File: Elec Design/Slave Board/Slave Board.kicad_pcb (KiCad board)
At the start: 2 copper layers, 81.3 x 358.6 mm, 93 parts, among them J3 OSTTC030162, J5 OSTTC030162, J6 0022232041, J7 Conn_ARM_JTAG_SWD_10, J8 OSTTC020162, J9 OSTTC020162, M1 Val**, M2 Val**, M3 Val**, M4 Val**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

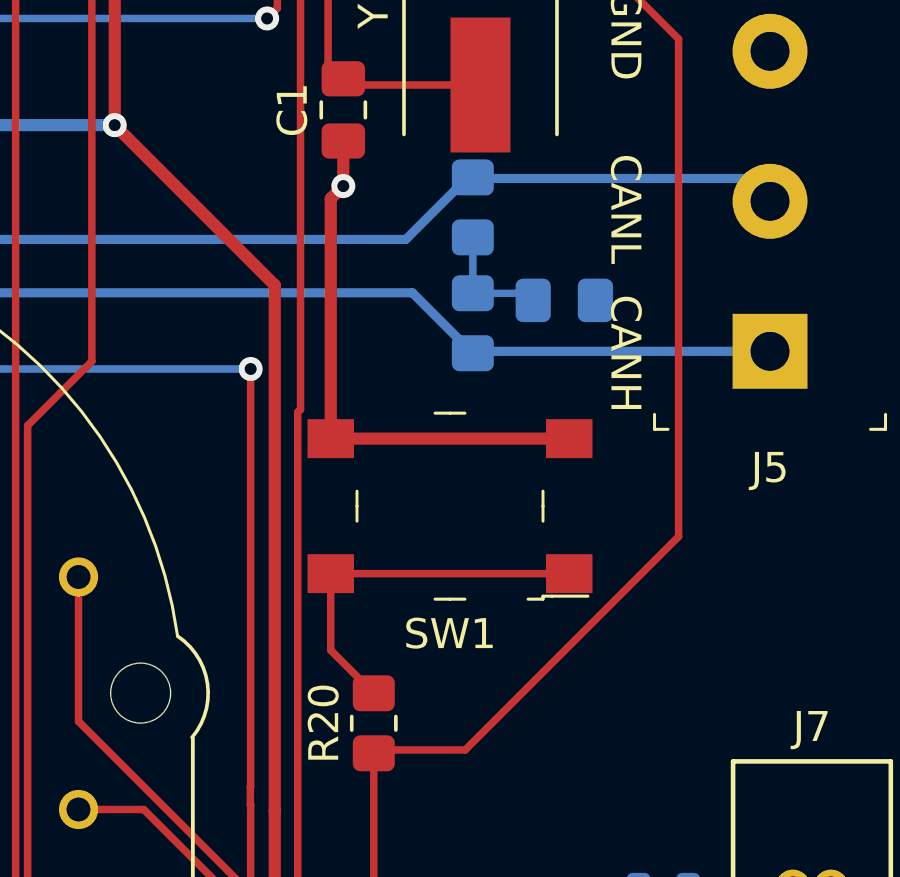
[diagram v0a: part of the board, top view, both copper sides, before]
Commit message: lining up with JLC parts
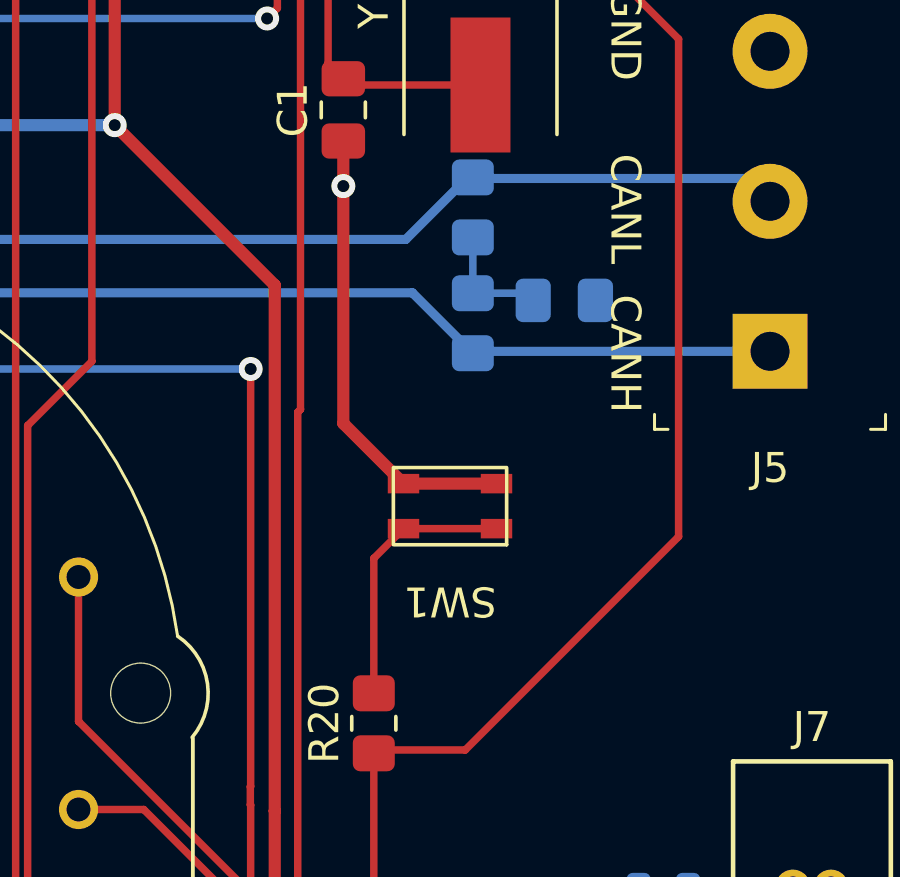
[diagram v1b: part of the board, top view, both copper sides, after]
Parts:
- SW1: footprint digikey-footprints:Switch_Tactile_SMD_6x6mm_PTS645 -> Switches:SW_SPST_ SKRPASE010
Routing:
- net Net-(R20-Pad2): track 12.5 -> 9.00 mm
- net GND: track 104.4 -> 101.7 mm

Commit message: further JLC alignment
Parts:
- J3, J5: value OSTTC030162 -> ~
- M1, M2, M3, M4: value Val** -> VID28-05
- U1: value LPC11C22_24-LQFP48 -> LPC11C24-LQFP48

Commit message: further bom alignment
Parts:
- C1, C10, C11, C12, C13, C16, C18, C19, C2, C21, C22, C23, C24, C3, C4, C5, C6, C7, C8, C9: footprint Capacitor_SMD:C_0805_2012Metric_Pad1.18x1.45mm_HandSolder -> Capacitor_SMD:C_0603_1608Metric
- C27, C28: value 0.1uF -> 100nF
- J3, J5: footprint digikey-footprints:Term_Block_1x3_P5mm -> TerminalBlock_Phoenix:TerminalBlock_Phoenix_PT-1,5-3-5.0-H_1x03_P5.00mm_Horizontal
- J6: value 0022232041 -> ~; footprint digikey-footprints:PinHeader_1x4_P2.54mm_Drill1.02mm -> Connector_PinHeader_2.54mm:PinHeader_1x04_P2.54mm_Vertical
- J7: footprint 10 pin jtag:CONN_3220-10-0100-00_CNC -> digikey-footprints:PinHeader_2x5_P1.27mm_Drill.7mm
- J8, J9: value OSTTC020162 -> ~; footprint digikey-footprints:Term_Block_1x2_P5mm -> TerminalBlock_Phoenix:TerminalBlock_Phoenix_PT-1,5-2-5.0-H_1x02_P5.00mm_Horizontal
- L1: footprint NR6028T4R7M:IND_NR6028T4R7M -> Inductors:IND_NR6028T4R7M
- R10, R11, R12, R13, R17, R18, R20, R29, R30, R5, R6, R7, R8, R9: footprint Resistor_SMD:R_0805_2012Metric_Pad1.20x1.40mm_HandSolder -> Resistor_SMD:R_0603_1608Metric
- R22: footprint Resistor_SMD:R_1206_3216Metric_Pad1.30x1.75mm_HandSolder -> Resistor_SMD:R_0603_1608Metric
- SW1: footprint Switches:SW_SPST_ SKRPASE010 -> Button_Switch_SMD:SW_SPST_PTS810
- U14: footprint BD9E302EFJ-E2:HTSOP-J8_ROM -> Buck Converter:HTSOP-J8_ROM
- moved Y1 9.86 mm to (261.6, 213.4)
- moved C1 8.87 mm to (256.5, 210.8)
- moved R20 3.56 mm to (269.7, 233.3)
- moved C2 2.29 mm to (259.3, 203.5)
- moved C3 2.29 mm to (261.6, 203.5)
- moved SW1 1.48 mm to (270.2, 226.0)
- moved J3 0.78 mm to (208.8, 211.4)
- moved C33 0.76 mm to (211.8, 171.2)
- moved D5 0.76 mm to (208.8, 192.3)
- moved J5 0.72 mm to (278.9, 221.4)
- moved J8 0.51 mm to (208.8, 199.9)
- moved J9 0.50 mm to (278.9, 204.9)
- turned J6 to 0 degrees
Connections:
- R20 pad 2: Net-(R20-Pad2) -> Net-(SW1-A)
- SW1 pad 1: Net-(R20-Pad2) -> Net-(SW1-A)
- SW1 pad 2: Net-(R20-Pad2) -> GND
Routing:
- net /RESET: track 76.5 -> 61.9 mm
- net +3.3V: track 813.5 -> 825.1 mm
- net Net-(SW1-A): track 0.00 -> 10.3 mm
- net Net-(R20-Pad2): track 9.00 -> 0.00 mm
- net GND: track 101.7 -> 94.6 mm, vias 24 -> 25
- net Net-(U1-XTALOUT): track 24.2 -> 17.8 mm, vias 3 -> 0
- net Net-(U1-XTALIN): track 26.1 -> 21.1 mm, vias 2 -> 0
- net VBUS: track 110.1 -> 107.9 mm
- net /HAll B Hour - 2: track 184.9 -> 182.7 mm
- net /CW/~{CCWC} - 2: track 127.8 -> 126.3 mm
- net /Driver Reset: track 243.9 -> 245.2 mm
- net /CANL: track 114.0 -> 112.9 mm
- net /HAll B Hour - 1: track 81.7 -> 82.7 mm
- net Net-(D5-A): track 19.1 -> 18.1 mm
- net Net-(U1-PIO3_0/~{DTR}): track 2.68 -> 3.31 mm
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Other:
- board text added: "Slave Board V1.1"

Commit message: minor bom changes
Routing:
- net +3.3V: track 825.1 -> 827.1 mm
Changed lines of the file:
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@@
 			)
 		)
+		(property "JLC PN" "C3819953"
+			(at 0 0 -90)
+			(unlocked yes)
+			(layer "F.Fab")
+			(hide yes)
+			(effects
+				(font
+					(size 1 1)
+					(thickness 0.15)
+				)
+			)
+		)
 		(sheetname "Root")
 		(sheetfile "Slave Board.kicad_sch")
@@
 			)
 		)
-		(property "MPN" "LPC11C24FBD48"
+		(property "MPN" "C1020252"
 			(at 0 0 180)
 			(unlocked yes)
@@
 			)
 		)
+		(property "JLC PN" "C2992620"
+			(at 0 0 -90)
+			(unlocked yes)
+			(layer "F.Fab")
+			(hide yes)
+			(effects
+				(font
+					(size 1 1)
+					(thickness 0.15)
+				)
+			)
+		)
 		(property ki_fp_filters "C_*")
 		(sheetname "Root")
@@
 			)
 		)
+		(property "JLC PN" "C3819953"
+			(at 0 0 90)
+			(unlocked yes)
+			(layer "F.Fab")
+			(hide yes)
+			(effects
+				(font
+					(size 1 1)
+					(thickness 0.15)
+				)
+			)
+		)
 		(sheetname "Root")
 		(sheetfile "Slave Board.kicad_sch")
@@
 			)
 		)
-		(property "Datasheet" "https://www.diodes.com/assets/Datasheets/B320AE/B340AE.pdf"
+		(property "Datasheet" "https://www.lcsc.com/datasheet/lcsc_datasheet_2307101649_MDD-Microdiode-Electronics-B340A_C64982.pdf"
 			(at 0 0 90)
 			(unlocked yes)
@@
 			)
 		)
-		(property "MPN" "B340AE"
+		(property "MPN" "C64982"
 			(at 0 0 0)
 			(layer "F.Fab")
@@
 			)
 		)
+		(property "JLC PN" "C2992620"
+			(at 0 0 0)
+			(unlocked yes)
+			(layer "F.Fab")
+			(hide yes)
+			(effects
+				(font
+					(size 1 1)
+					(thickness 0.15)
+				)
+			)
+		)
 		(property ki_fp_filters "C_*")
 		(sheetname "Root")
@@
 			)
 		)
+		(property "MPN" "C2891841"
+			(at 0 0 90)
+			(unlocked yes)
+			(layer "F.Fab")
+			(hide yes)
+			(effects
+				(font
+					(size 1 1)
+					(thickness 0.15)
+				)
+			)
+		)
 		(property ki_fp_filters "SOT?23*")
 		(sheetname "Root")
@@
 		(tags "resistor")
 		(property "Reference" "R30"
-			(at 0 -1.43 0)
+			(at 0.127 1.651 0)
 			(layer "F.SilkS")
 			(effects
@@
 		(tags "capacitor")
 		(property "Reference" "C24"
-			(at 0 -1.43 90)
+			(at 0.127 1.651 90)
 			(layer "F.SilkS")
 			(effects
@@
 		(tags "capacitor")
 		(property "Reference" "C16"
-			(at 0 -1.43 0)
+			(at 0 1.524 0)
 			(layer "F.SilkS")
 			(effects
@@
 		(tags "capacitor")
 		(property "Reference" "C18"
-			(at 0 -1.43 180)
+			(at 0 1.524 180)
 			(layer "F.SilkS")
 			(effects
@@
 		(tags "capacitor")
 		(property "Reference" "C21"
-			(at 0 -1.43 90)
+			(at 0.127 1.524 90)
 			(layer "F.SilkS")
 			(effects
@@
 			)
 		)
+		(property "MPN" "C919448"
+			(at 0 0 90)
+			(unlocked yes)
+			(layer "F.Fab")
+			(hide yes)
+			(effects
+				(font
+					(size 1 1)
+					(thickness 0.15)
+				)
+			)
+		)
+		(property "JLC PN" "C919448"
+			(at 0 0 90)
+			(unlocked yes)
+			(layer "F.Fab")
+			(hide yes)
+			(effects
+				(font
+					(size 1 1)
+					(thickness 0.15)
+				)
+			)
+		)
 		(property ki_fp_filters "HTSOP-J8_ROM HTSOP-J8_ROM-M HTSOP-J8_ROM-L")
 		(sheetname "Root")
@@
 		(tags "capacitor")
 		(property "Reference" "C5"
-			(at 0 -1.43 180)
+			(at 0.127 1.397 180)
 			(layer "F.SilkS")
 			(effects
@@
 			)
 		)
+		(property "JLC PN" "C77758"
+			(at 0 0 180)
+			(unlocked yes)
+			(layer "F.Fab")
+			(hide yes)
+			(effects
+				(font
+					(size 1 1)
+					(thickness 0.15)
+				)
+			)
+		)
 		(property ki_fp_filters "Choke_* *Coil* Inductor_* L_*")
 		(sheetname "Root")
@@
 			)
 		)
-		(property "MPN" "PTS810SJS250SMTRLFS"
+		(property "MPN" "C221897"
 			(at 0 0 180)
 			(unlocked yes)
@@
 			)
 		)
-		(property "Datasheet" "https://connect.kemet.com:7667/gateway/IntelliData-ComponentDocumentation/1.0/download/datasheet/C0603C104K5RECAUTO"
+		(property "Datasheet" ""
 			(at 0 0 0)
 			(unlocked yes)
@@
 			)
 		)
-		(property "JLC?" "N"
+		(property "MPN" "GRM188R6YA106MA73J"
 			(at 0 0 0)
 			(layer "F.Fab")
@@
 			)
 		)
-		(property "MPN" "C0603C104K5RECAUTO"
+		(property "Rated V" "35V"
 			(at 0 0 0)
 			(layer "F.Fab")
@@
 			)
 		)
-		(property "Rated V" "50V"
+		(property "JLC PN" "C2244191"
 			(at 0 0 0)
+			(unlocked yes)
 			(layer "F.Fab")
 			(hide yes)
@@
 			)
 		)
+		(property "JLC PN" "C3816891"
+			(at 0 0 90)
+			(unlocked yes)
+			(layer "F.Fab")
+			(hide yes)
+			(effects
+				(font
+					(size 1 1)
+					(thickness 0.15)
+				)
+			)
+		)
 		(sheetname "Root")
 		(sheetfile "Slave Board.kicad_sch")
@@
 			)
 		)
+		(property "JLC PN" "C2975357"
+			(at 0 0 -90)
+			(unlocked yes)
+			(layer "F.Fab")
+			(hide yes)
+			(effects
+				(font
+					(size 1 1)
+					(thickness 0.15)
+				)
+			)
+		)
+		(property "MPN" "C2975357"
+			(at 0 0 -90)
+			(unlocked yes)
+			(layer "F.Fab")
+			(hide yes)
+			(effects
+				(font
+					(size 1 1)
+					(thickness 0.15)
+				)
+			)
+		)
 		(property ki_fp_filters "Crystal*")
 		(sheetname "Root")
@@
 		(tags "capacitor")
 		(property "Reference" "C3"
-			(at 0 -1.43 90)
+			(at 0.173 1.651 90)
 			(layer "F.SilkS")
 			(effects
@@
 			)
 		)
+		(property "JLC PN" "C3816891"
+			(at 0 0 -90)
+			(unlocked yes)
+			(layer "F.Fab")
+			(hide yes)
+			(effects
+				(font
+					(size 1 1)
+					(thickness 0.15)
+				)
+			)
+		)
 		(sheetname "Root")
 		(sheetfile "Slave Board.kicad_sch")
@@
 		(tags "resistor")
 		(property "Reference" "R13"
-			(at 0 1.43 0)
+			(at 0 -1.524 0)
 			(layer "B.SilkS")
 			(effects
@@
 		(tags "resistor")
 		(property "Reference" "R5"
-			(at 0 1.43 90)
+			(at 0.127 -1.524 90)
 			(layer "B.SilkS")
 			(effects
@@
 		(tags "resistor")
 		(property "Reference" "R12"
-			(at 0 1.43 0)
+			(at 0 -1.651 0)
 			(layer "B.SilkS")
 			(effects
@@
 		(tags "resistor")
 		(property "Reference" "R8"
-			(at 0 1.43 0)
+			(at 0 -1.397 0)
 			(layer "B.SilkS")
 			(effects
@@
 	)
 	(segment
+		(start 206.8575 151.342)
+		(end 206.8575 149.4405)
+		(width 0.4064)
+		(layer "B.Cu")
+		(net 4)
+	)
+	(segment
 		(start 263.398 149.352)
 		(end 264.938 149.352)
@@
 	)
 	(segment
+		(start 206.8575 149.4405)
+		(end 206.769 149.352)
+		(width 0.4064)
+		(layer "B.Cu")
+		(net 4)
+	)
+	(segment
 		(start 263.398 154.686)
 		(end 263.906 155.194)
@@
 	)
 	(segment
-		(start 243.4805 194.14)
-		(end 243.459 194.1615)
-		(width 0.2)
-		(layer "F.Cu")
-		(net 5)
-	)
-	(segment
-		(start 242.593 194.9435)
-		(end 242.593 198.778)
+		(start 243.4805 194.056)
+		(end 242.443 195.0935)
 		(width 0.2)
 		(layer "F.Cu")
@@
 	)
 	(segment
-		(start 243.459 199.644)
-		(end 244.106 200.291)
+		(start 244.106 200.291)
+		(end 244.106 200.30167)
 		(width 0.2)
 		(layer "F.Cu")
@@
 	)
 	(segment
-		(start 243.4805 194.056)
-		(end 243.4805 194.14)
+		(start 243.4805 194.14)
+		(end 243.459 194.1615)
 		(width 0.2)
 		(layer "F.Cu")
@@
 	)
 	(segment
-		(start 242.593 198.778)
-		(end 243.459 199.644)
+		(start 242.443 195.0935)
+		(end 242.443 198.628)
 		(width 0.2)
 		(layer "F.Cu")
@@
 	)
 	(segment
-		(start 244.106 200.291)
-		(end 244.106 200.30167)
+		(start 242.443 198.628)
+		(end 244.106 200.291)
 		(width 0.2)
 		(layer "F.Cu")
@@
 	(segment
 		(start 243.4805 194.056)
-		(end 242.593 194.9435)
+		(end 243.4805 194.14)
 		(width 0.2)
 		(layer "F.Cu")

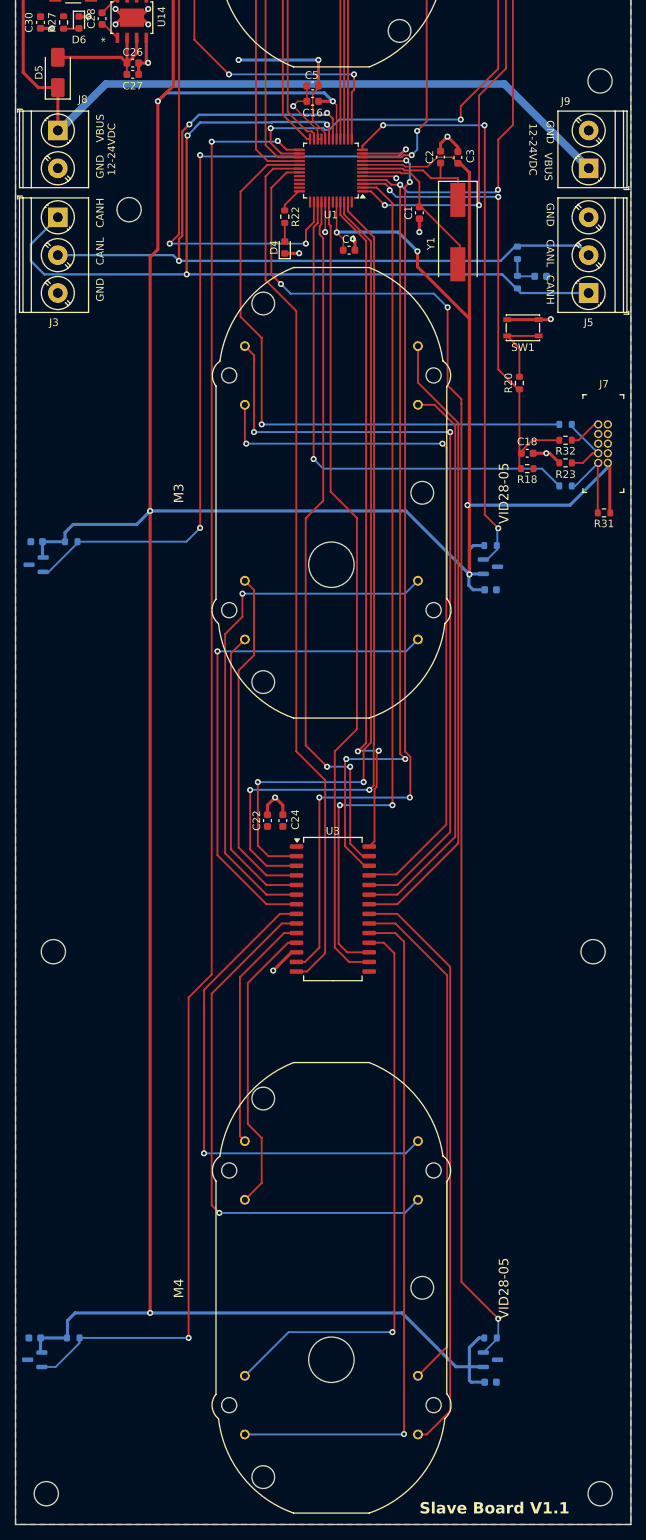
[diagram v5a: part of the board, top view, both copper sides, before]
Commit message: corrected barrier diode direction on both boards
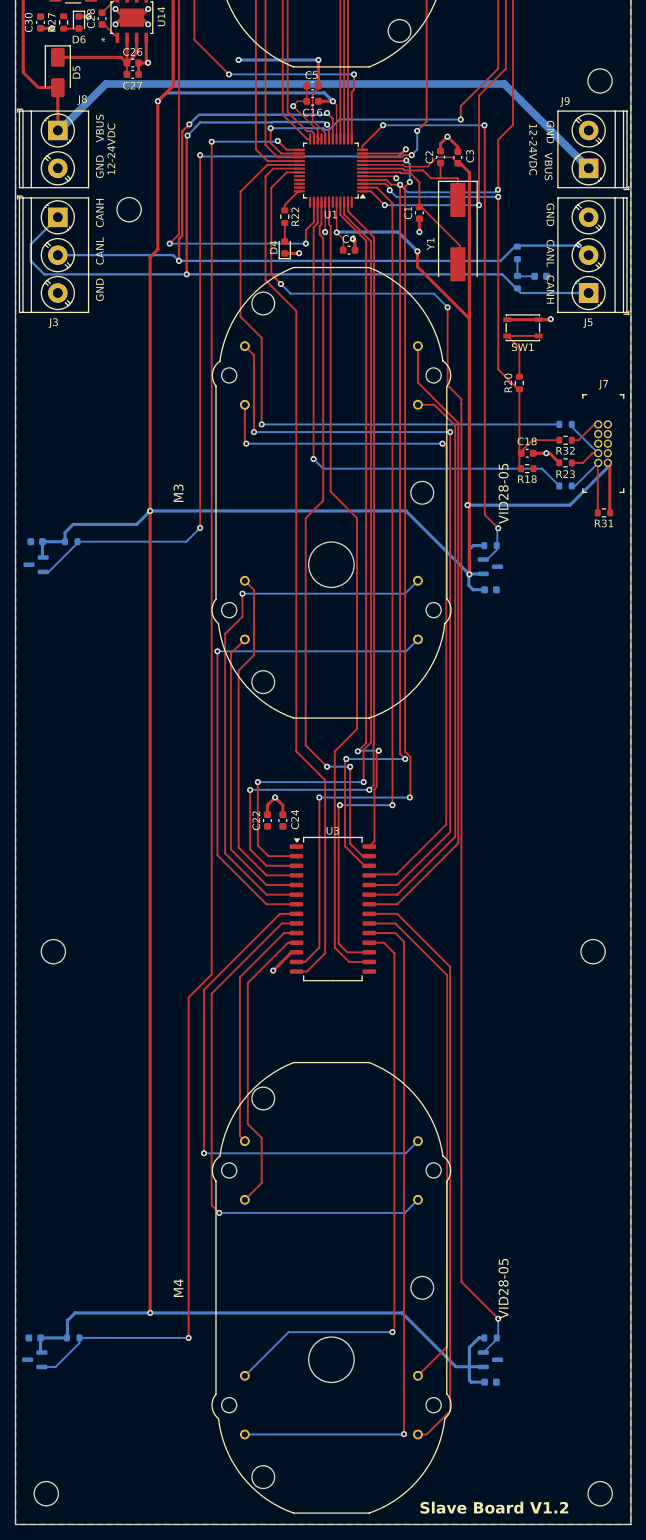
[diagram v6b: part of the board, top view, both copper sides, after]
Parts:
- J3: value ~ -> 1935174
- J6: value ~ -> 61300411121
- J8, J9: value ~ -> 1935161
- turned D5 to -90 degrees
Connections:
- C26 pad 1: Net-(D5-A) -> Net-(D5-K)
- C27 pad 1: Net-(D5-A) -> Net-(D5-K)
- D5 pad 1: VBUS -> Net-(D5-K)
- D5 pad 2: Net-(D5-A) -> VBUS
- U14 pad 2: Net-(D5-A) -> Net-(D5-K)
- U14 pad 3: Net-(D5-A) -> Net-(D5-K)
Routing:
- net Net-(D5-K): track 0.00 -> 18.1 mm
- net Net-(D5-A): track 18.1 -> 0.00 mm
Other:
- board text added: "Slave Board V1.2"
- board text removed: "Slave Board V1.1"
